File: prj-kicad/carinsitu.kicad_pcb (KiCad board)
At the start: 2 copper layers, 120 x 50 mm, 73 parts, among them P1 BAT, P2 MOT, P3 CONN_3, P4 CONN_4, Q1 TJ15P04M3, SW1 SWITCH_SLIDE, SW2 Reset, U1 LoLin_D1_mini_pro, U2 MIC2860, U3 MAX17044G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

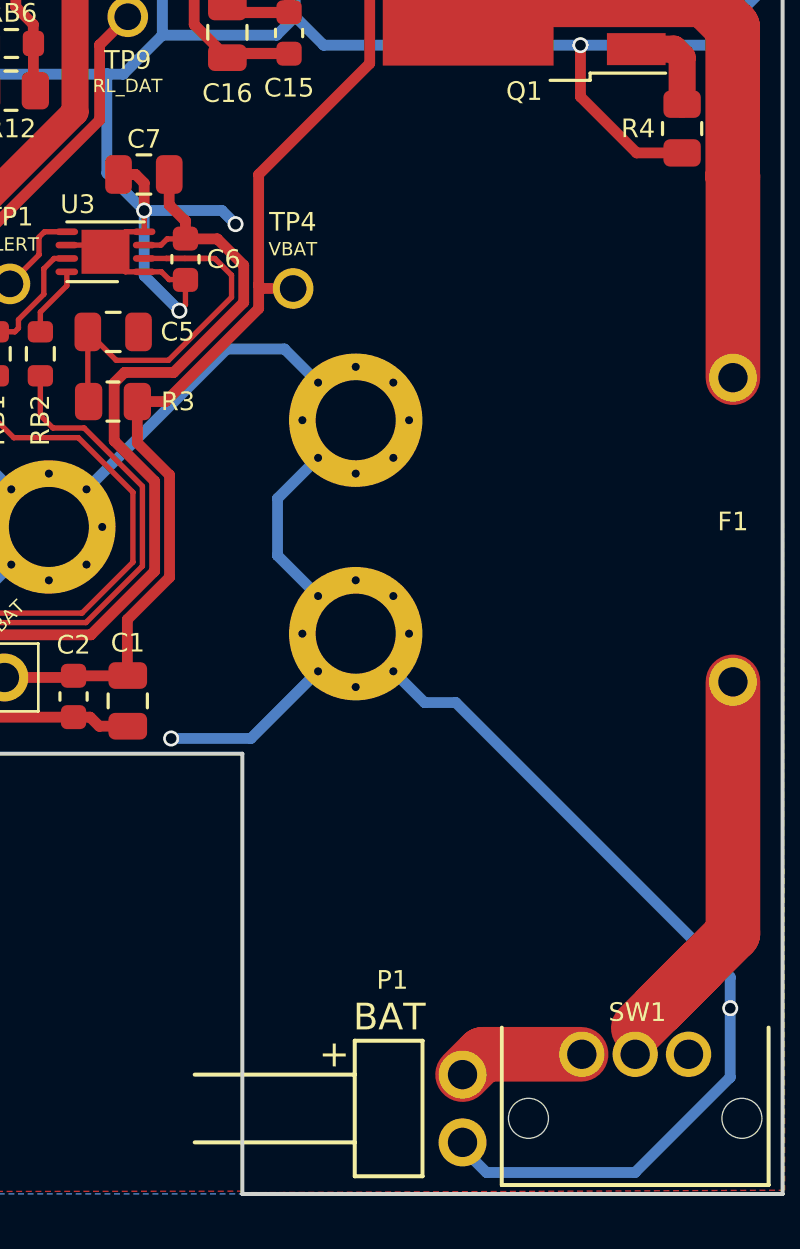
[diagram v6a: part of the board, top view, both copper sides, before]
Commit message: Move VTX holes slightly + adjust around BAT connector
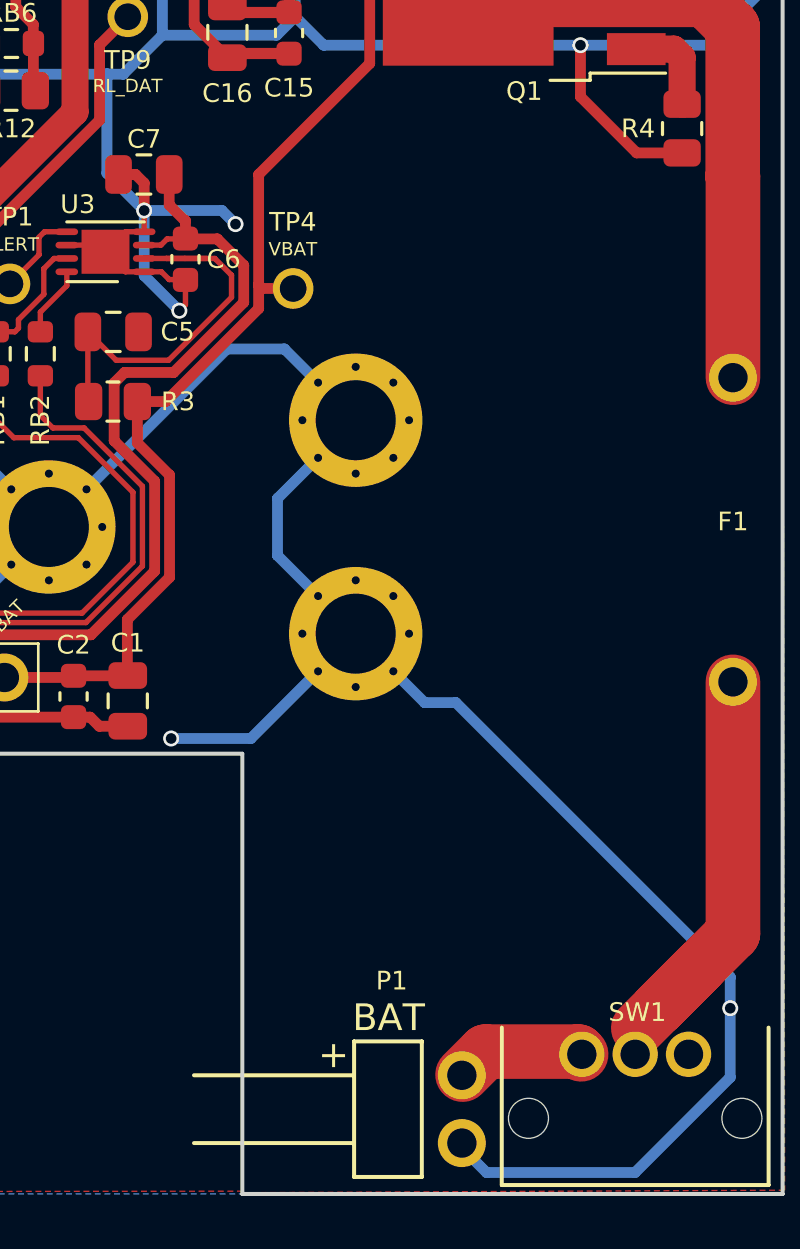
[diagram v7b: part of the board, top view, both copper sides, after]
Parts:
- moved H1 0.75 mm to (180.2, 105.0)
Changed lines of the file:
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@@
   )
   (footprint "carinsitu:CONN_61300211021" (layer "F.Cu")
-    (at 190.754 126.7968 -90)
+    (at 190.7286 126.8222 -90)
     (property "Distrib Ref" "2356176")
     (property "Distributor" "Farnell")
@@
   )
   (footprint "carinsitu:VTX_avatar_halfholes" (layer "F.Cu")
-    (at 181 105)
+    (at 180.25 105)
     (property "Sheetfile" "carinsitu.kicad_sch")
     (property "Sheetname" "")
@@
   (segment (start 197.2244 123.899037) (end 197.340918 123.782519) (width 1.016) (layer "F.Cu") (net 49))
   (segment (start 199.679 121.444438) (end 198.102919 123.020519) (width 2.048) (layer "F.Cu") (net 49))
-  (segment (start 191.516 124.7648) (end 190.754 125.5268) (width 2.048) (layer "F.Cu") (net 50))
-  (segment (start 195.198 124.7648) (end 191.516 124.7648) (width 2.048) (layer "F.Cu") (net 50))
+  (segment (start 195.198 124.7648) (end 195.0964 124.6632) (width 2.048) (layer "F.Cu") (net 50))
+  (segment (start 195.0964 124.6632) (end 191.6176 124.6632) (width 2.048) (layer "F.Cu") (net 50))
+  (segment (start 191.6176 124.6632) (end 190.754 125.5268) (width 2.048) (layer "F.Cu") (net 50))
   (zone (net 1) (net_name "GND") (layer "F.Cu") (hatch edge 0.508)
     (connect_pads (clearance 0.2))

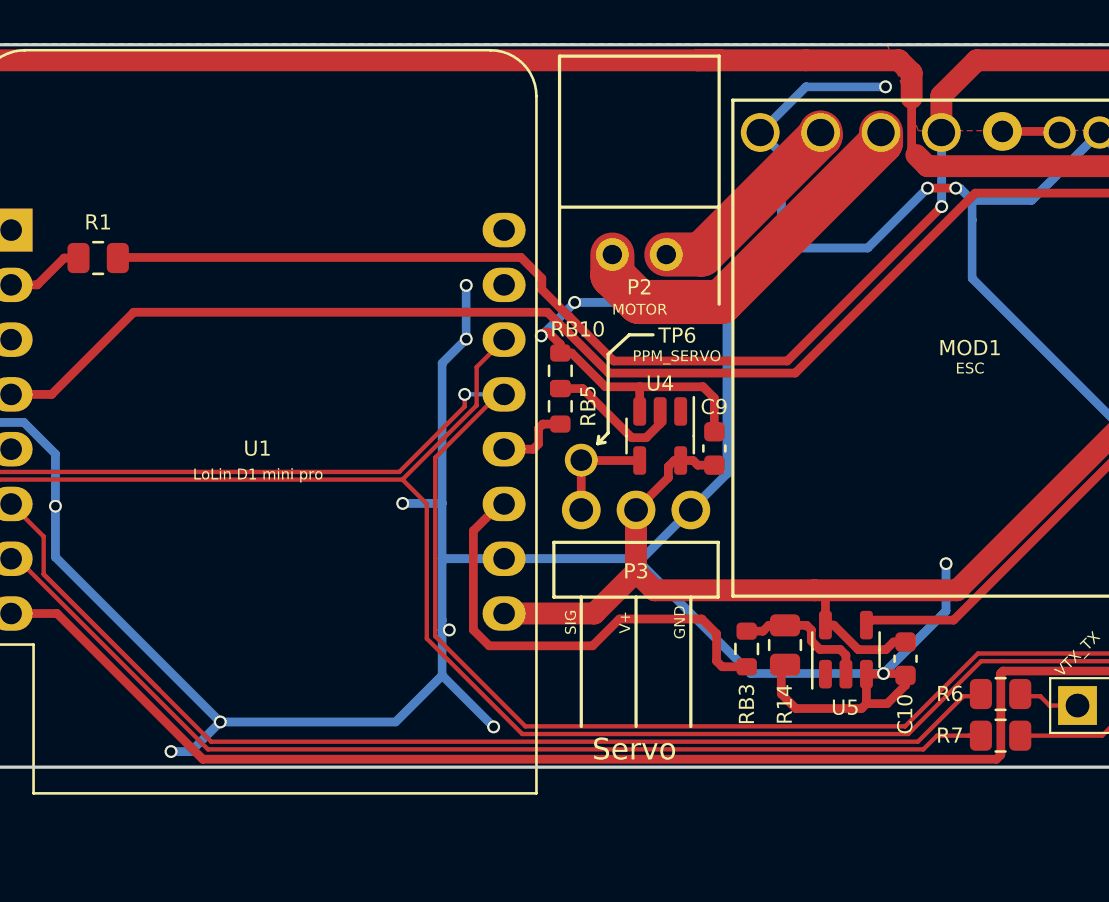
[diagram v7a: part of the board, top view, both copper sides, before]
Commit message: Move Servo connector out of spacer + invert Motor connector to gain place
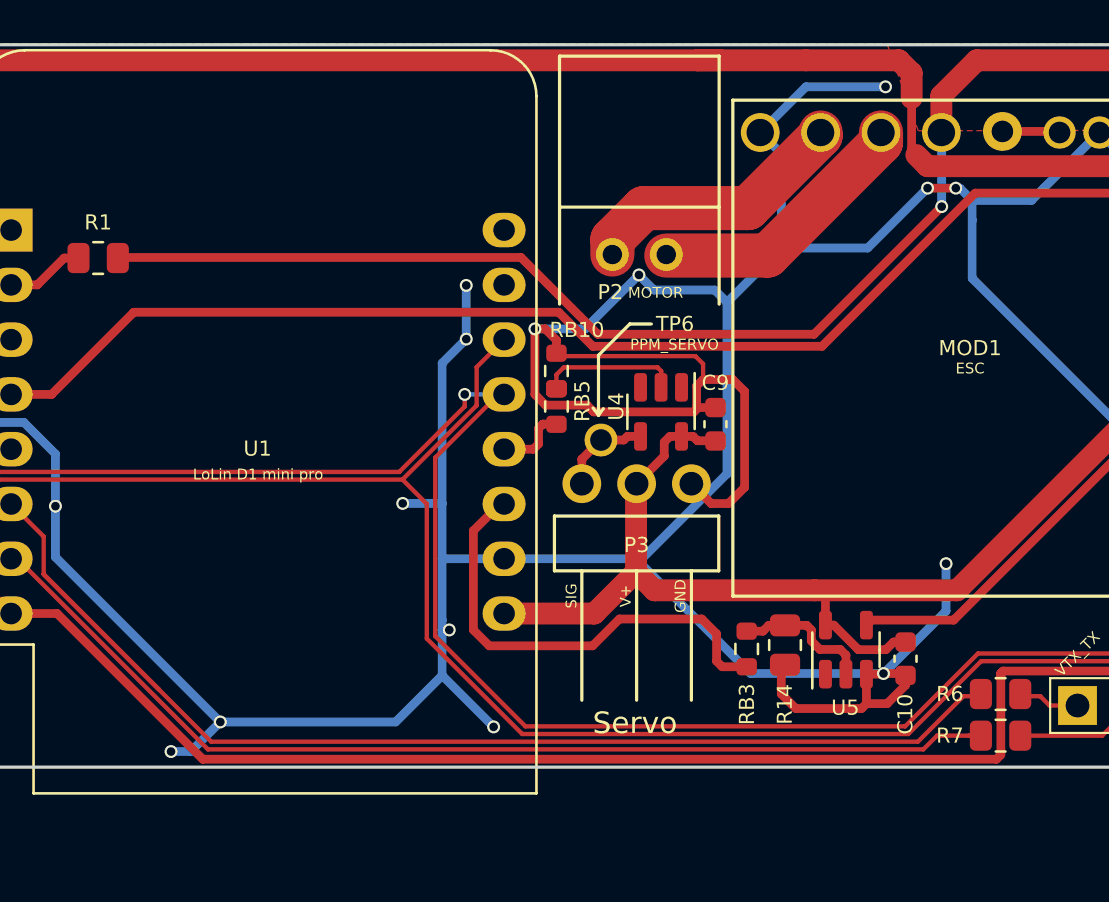
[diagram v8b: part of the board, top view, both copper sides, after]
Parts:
- moved TP6 1.31 mm to (143.9, 98.3)
- moved P3 1.22 mm to (145.5, 100.4)
- moved C9 1.12 mm to (149.2, 97.6)
- moved U4 1.12 mm to (146.7, 97.0)
- moved RB5 0.18 mm to (141.8, 96.8)
- moved RB10 0.18 mm to (141.8, 95.1)
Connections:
- P2 pad 1: Net-(MOD1-Pad2) -> Net-(MOD1-Pad3)
- P2 pad 2: Net-(MOD1-Pad3) -> Net-(MOD1-Pad2)
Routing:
- net GND: track 507.3 -> 528.6 mm
- net Net-(MOD1-Pad3): track 17.4 -> 12.6 mm
- net Net-(MOD1-Pad2): track 9.58 -> 12.5 mm
- net +VBAT: track 133.9 -> 132.6 mm
- net Net-(RB6-Pad1): track 62.7 -> 61.7 mm
- net +5V: track 243.4 -> 242.5 mm
- net Net-(P3-Pad1): track 5.00 -> 4.30 mm
